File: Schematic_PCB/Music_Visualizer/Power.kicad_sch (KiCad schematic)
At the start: 15 parts, among them J2 PJ-079BH, SW2 SW_SPST, U8 LT1054, U9 MC78L05_TO92

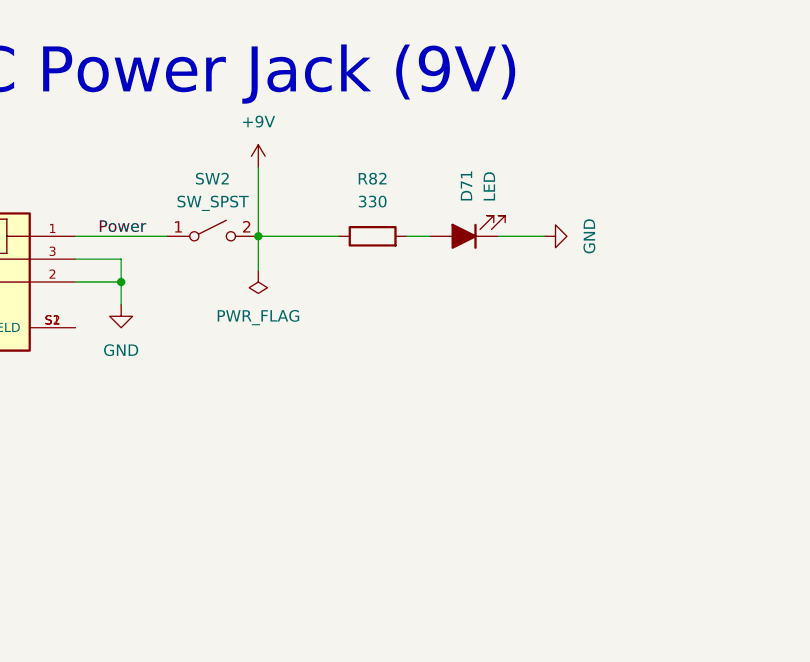
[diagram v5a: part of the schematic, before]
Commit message: Re-oriented Power Indicator circuit
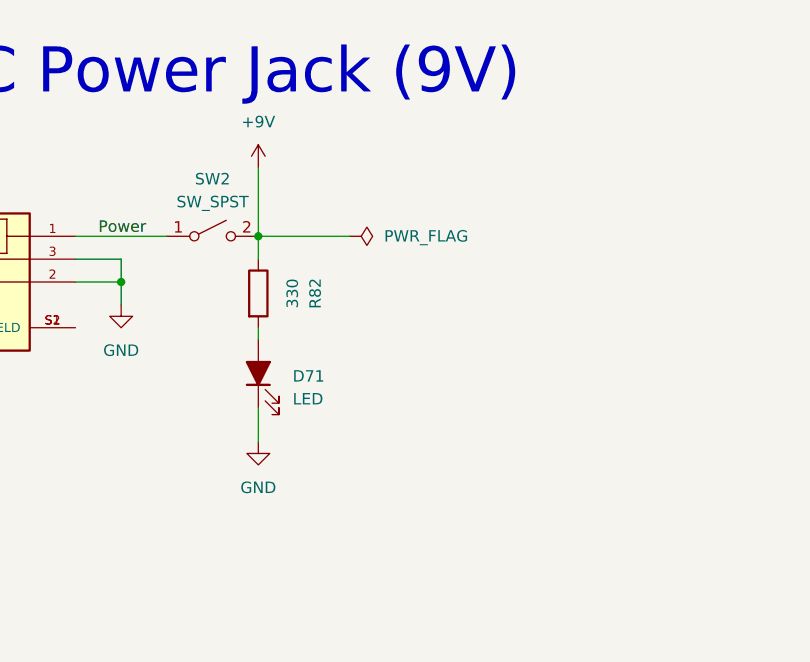
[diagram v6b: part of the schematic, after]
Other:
- moved on the sheet: D71, R82
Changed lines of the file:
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@@
-    (stroke (width 0) (type default) (color 0 0 0 0))
-  )
-  (wire (pts (xy 64.77 52.07) (xy 73.66 52.07))
     (stroke (width 0) (type default) (color 0 0 0 0))
   )
@@
     (stroke (width 0) (type default) (color 0 0 0 0))
   )
+  (wire (pts (xy 64.77 52.07) (xy 64.77 54.61))
+    (stroke (width 0) (type default) (color 0 0 0 0))
+  )
   (wire (pts (xy 162.56 48.26) (xy 162.56 50.8))
     (stroke (width 0) (type default) (color 0 0 0 0))
@@
     (stroke (width 0) (type default) (color 0 0 0 0))
   )
-  (wire (pts (xy 64.77 55.88) (xy 64.77 52.07))
-    (stroke (width 0) (type default) (color 0 0 0 0))
-  )
   (wire (pts (xy 95.25 138.43) (xy 99.06 138.43))
     (stroke (width 0) (type default) (color 0 0 0 0))
@@
     (stroke (width 0) (type default) (color 0 0 0 0))
   )
-  (wire (pts (xy 91.44 52.07) (xy 96.52 52.07))
+  (wire (pts (xy 64.77 71.12) (xy 64.77 74.93))
     (stroke (width 0) (type default) (color 0 0 0 0))
   )
@@
     (stroke (width 0) (type default) (color 0 0 0 0))
   )
-  (wire (pts (xy 81.28 52.07) (xy 83.82 52.07))
+  (wire (pts (xy 74.93 52.07) (xy 64.77 52.07))
+    (stroke (width 0) (type default) (color 0 0 0 0))
+  )
+  (wire (pts (xy 64.77 62.23) (xy 64.77 63.5))
     (stroke (width 0) (type default) (color 0 0 0 0))
   )
@@
     (pin "2")
   )
-  (symbol (lib_id "Device:R") (at 77.47 52.07 90) (unit 1)
-    (in_bom yes) (on_board yes) (fields_autoplaced)
-    (property "Reference" "R82" (id 0) (at 77.47 45.72 90))
-    (property "Value" "330" (id 1) (at 77.47 48.26 90))
-    (property "Footprint" "Resistor_SMD:R_0603_1608Metric" (id 2) (at 77.47 53.848 90)
-      (effects (font (size 1.27 1.27)) hide)
-    )
-    (property "Datasheet" "https://fscdn.rohm.com/en/products/databook/datasheet/passive/resistor/chip_resistor/sdr-e.pdf" (id 3) (at 77.47 52.07 0)
-      (effects (font (size 1.27 1.27)) hide)
-    )
-    (pin "1")
-    (pin "2")
-  )
-  (symbol (lib_id "User_Global_Symbol_Library:LED") (at 87.63 52.07 180) (unit 1)
-    (in_bom yes) (on_board yes) (fields_autoplaced)
-    (property "Reference" "D71" (id 0) (at 87.9474 48.26 90)
+  (symbol (lib_id "Device:R") (at 64.77 58.42 0) (unit 1)
+    (in_bom yes) (on_board yes) (fields_autoplaced)
+    (property "Reference" "R82" (id 0) (at 71.12 58.42 90))
+    (property "Value" "330" (id 1) (at 68.58 58.42 90))
+    (property "Footprint" "Resistor_SMD:R_0603_1608Metric" (id 2) (at 62.992 58.42 90)
+      (effects (font (size 1.27 1.27)) hide)
+    )
+    (property "Datasheet" "https://fscdn.rohm.com/en/products/databook/datasheet/passive/resistor/chip_resistor/sdr-e.pdf" (id 3) (at 64.77 58.42 0)
+      (effects (font (size 1.27 1.27)) hide)
+    )
+    (pin "1")
+    (pin "2")
+  )
+  (symbol (lib_id "User_Global_Symbol_Library:LED") (at 64.77 67.31 90) (unit 1)
+    (in_bom yes) (on_board yes) (fields_autoplaced)
+    (property "Reference" "D71" (id 0) (at 68.58 67.6274 90)
       (effects (font (size 1.27 1.27)) (justify right))
     )
-    (property "Value" "LED" (id 1) (at 90.4874 48.26 90)
+    (property "Value" "LED" (id 1) (at 68.58 70.1674 90)
       (effects (font (size 1.27 1.27)) (justify right))
     )
-    (property "Footprint" "LED_THT:LED_D5.0mm" (id 2) (at 87.63 52.07 0)
-      (effects (font (size 1.27 1.27)) hide)
-    )
-    (property "Datasheet" "~" (id 3) (at 87.63 52.07 0)
+    (property "Footprint" "LED_THT:LED_D5.0mm" (id 2) (at 64.77 67.31 0)
+      (effects (font (size 1.27 1.27)) hide)
+    )
+    (property "Datasheet" "~" (id 3) (at 64.77 67.31 0)
       (effects (font (size 1.27 1.27)) hide)
     )
@@
     (pin "1")
   )
-  (symbol (lib_id "power:PWR_FLAG") (at 64.77 55.88 180) (unit 1)
-    (in_bom yes) (on_board yes) (fields_autoplaced)
-    (property "Reference" "#FLG01" (id 0) (at 64.77 57.785 0)
-      (effects (font (size 1.27 1.27)) hide)
-    )
-    (property "Value" "PWR_FLAG" (id 1) (at 64.77 60.96 0))
-    (property "Footprint" "" (id 2) (at 64.77 55.88 0)
-      (effects (font (size 1.27 1.27)) hide)
-    )
-    (property "Datasheet" "~" (id 3) (at 64.77 55.88 0)
+  (symbol (lib_id "power:PWR_FLAG") (at 74.93 52.07 270) (unit 1)
+    (in_bom yes) (on_board yes) (fields_autoplaced)
+    (property "Reference" "#FLG01" (id 0) (at 76.835 52.07 0)
+      (effects (font (size 1.27 1.27)) hide)
+    )
+    (property "Value" "PWR_FLAG" (id 1) (at 78.74 52.0699 90)
+      (effects (font (size 1.27 1.27)) (justify left))
+    )
+    (property "Footprint" "" (id 2) (at 74.93 52.07 0)
+      (effects (font (size 1.27 1.27)) hide)
+    )
+    (property "Datasheet" "~" (id 3) (at 74.93 52.07 0)
       (effects (font (size 1.27 1.27)) hide)
     )
@@
     (pin "1")
   )
-  (symbol (lib_id "power:GND") (at 96.52 52.07 90) (unit 1)
-    (in_bom yes) (on_board yes) (fields_autoplaced)
-    (property "Reference" "#PWR090" (id 0) (at 102.87 52.07 0)
-      (effects (font (size 1.27 1.27)) hide)
-    )
-    (property "Value" "GND" (id 1) (at 101.6 52.07 0))
-    (property "Footprint" "" (id 2) (at 96.52 52.07 0)
-      (effects (font (size 1.27 1.27)) hide)
-    )
-    (property "Datasheet" "" (id 3) (at 96.52 52.07 0)
-      (effects (font (size 1.27 1.27)) hide)
-    )
+  (symbol (lib_id "power:GND") (at 64.77 74.93 0) (unit 1)
+    (in_bom yes) (on_board yes) (fields_autoplaced)
+    (property "Reference" "#PWR090" (id 0) (at 64.77 81.28 0)
+      (effects (font (size 1.27 1.27)) hide)
+    )
+    (property "Value" "GND" (id 1) (at 64.77 80.01 0))
+    (property "Footprint" "" (id 2) (at 64.77 74.93 0)
+      (effects (font (size 1.27 1.27)) hide)
+    )
+    (property "Datasheet" "" (id 3) (at 64.77 74.93 0)
+      (effects (font (size 1.27 1.27)) hide)
+    )

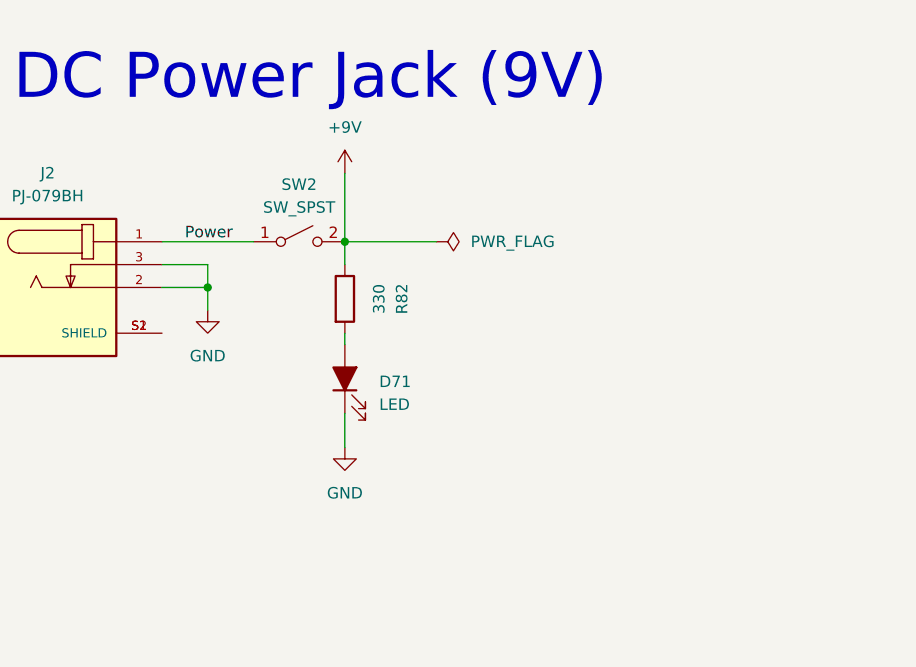
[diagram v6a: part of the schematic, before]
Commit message: Added pmos for reverse voltage protection
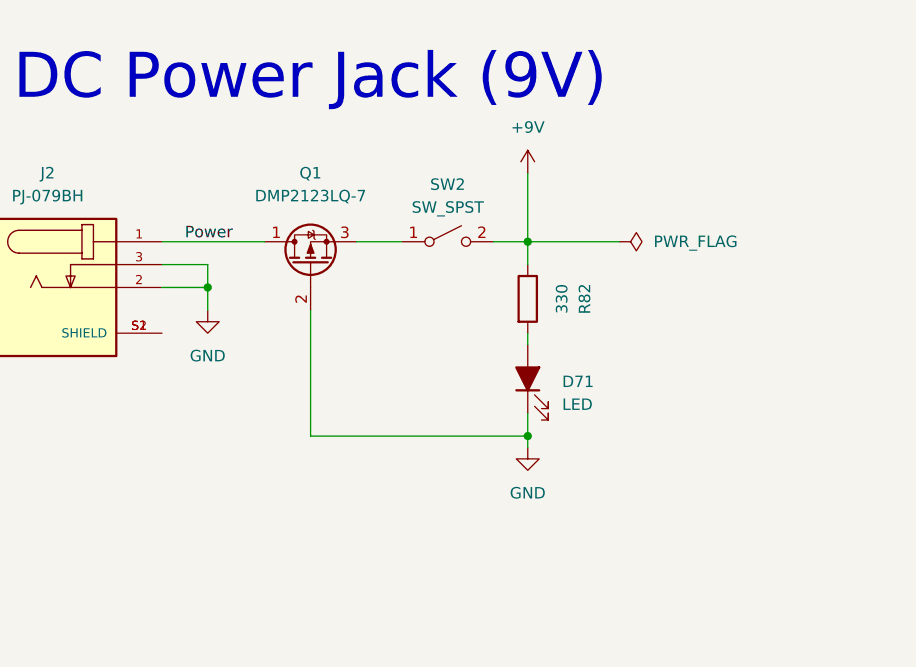
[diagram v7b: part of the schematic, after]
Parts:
- added Q1: DMP2123LQ-7, Package_TO_SOT_SMD:SOT-23, symbol Device:Q_PMOS_DGS
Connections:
- net GND: now also Q1.2 (G)
- net Power: now also Q1.1 (D); no longer SW2.1 (A)
- new net: Q1.3 (S), SW2.1 (A)
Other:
- moved on the sheet: D71, R82, SW2

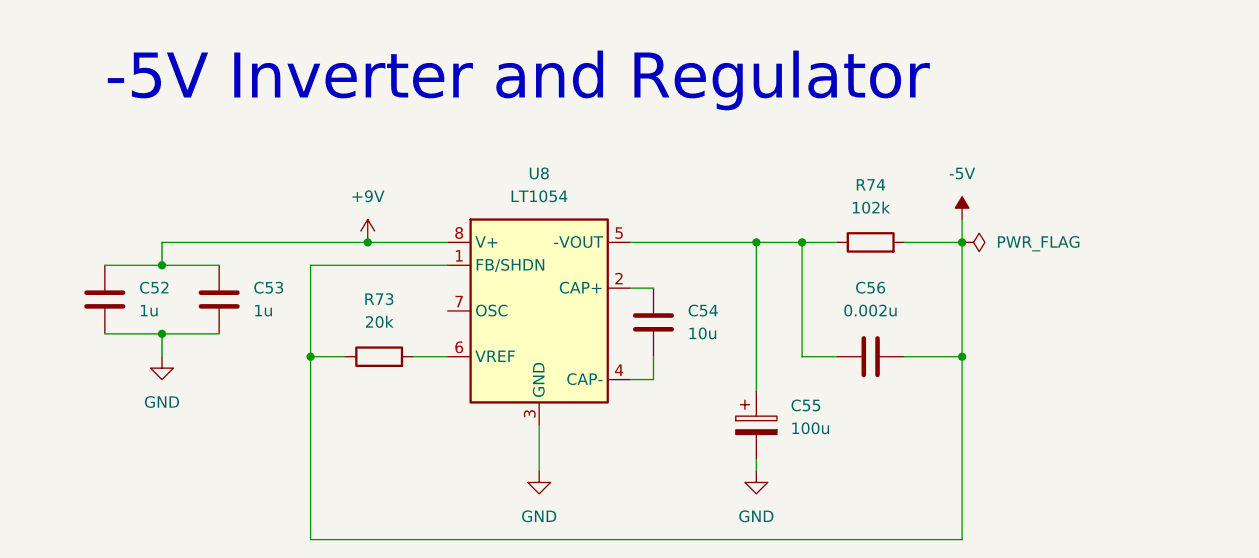
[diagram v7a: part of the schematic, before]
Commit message: Corrected LT1054 -5V power output label placement, identified which components are 0201 and corrected digi number and page of C-47,48,49,52,53,58 1u caps
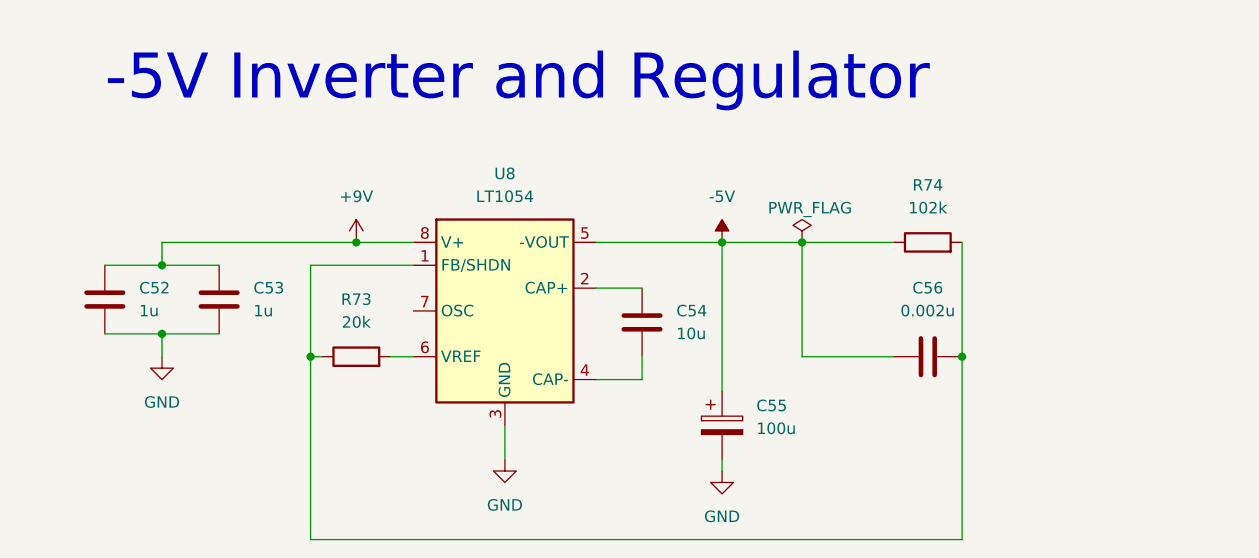
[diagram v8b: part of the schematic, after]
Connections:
- net -5V: now also C55.1, C56.1, R74.1, U8.5 (-VOUT); no longer C56.2, R73.1, R74.2, U8.1 (FB/SHDN)
- new net: C56.2, R73.1, R74.2, U8.1 (FB/SHDN)
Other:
- moved on the sheet: C54, C55, C56, R73, R74, U8
